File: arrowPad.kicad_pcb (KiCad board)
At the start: 2 copper layers, 28 parts, among them K1 KEYSW, K2 KEYSW, K3 KEYSW, K4 KEYSW, K5 KEYSW, K6 KEYSW, K7 KEYSW, K8 KEYSW, K9 KEYSW, SW1 SW_DIP_x01, U1 ProMicro, U2 NRF24L01_Breakout

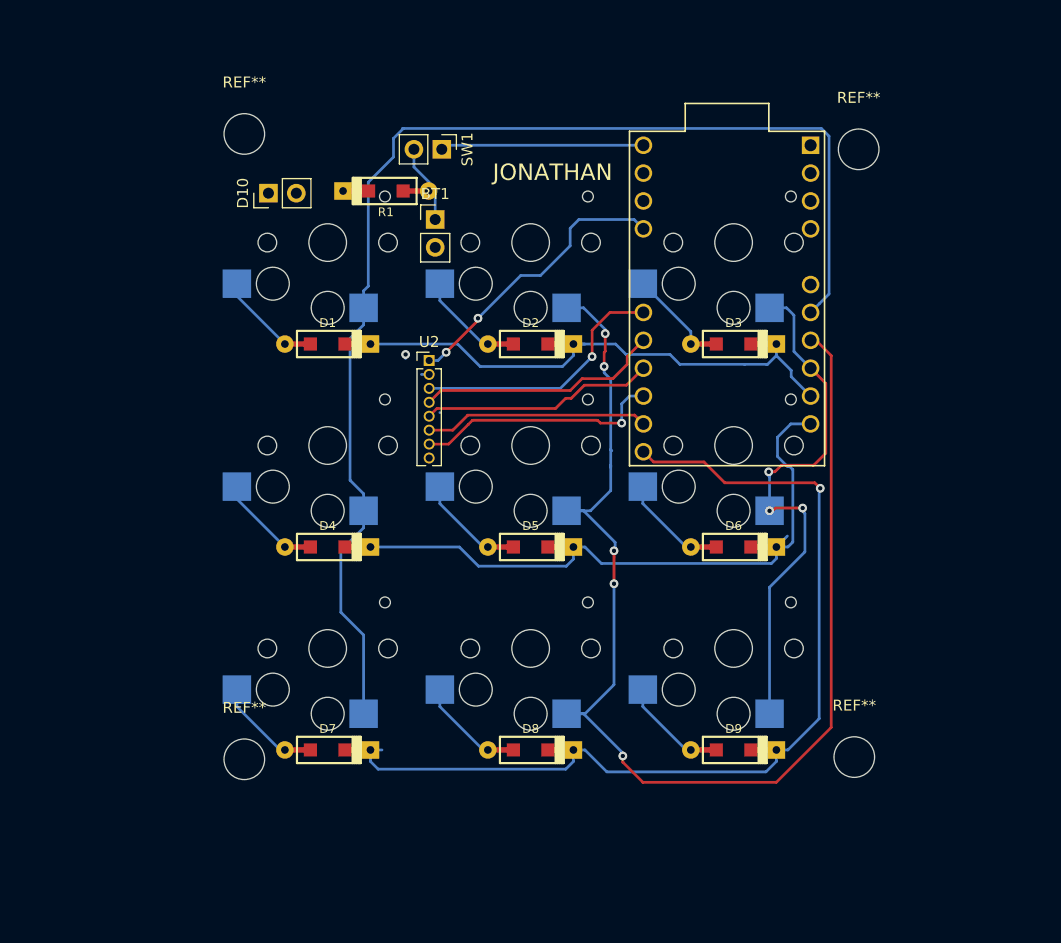
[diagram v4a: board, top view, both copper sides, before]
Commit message: added wired communication between boards
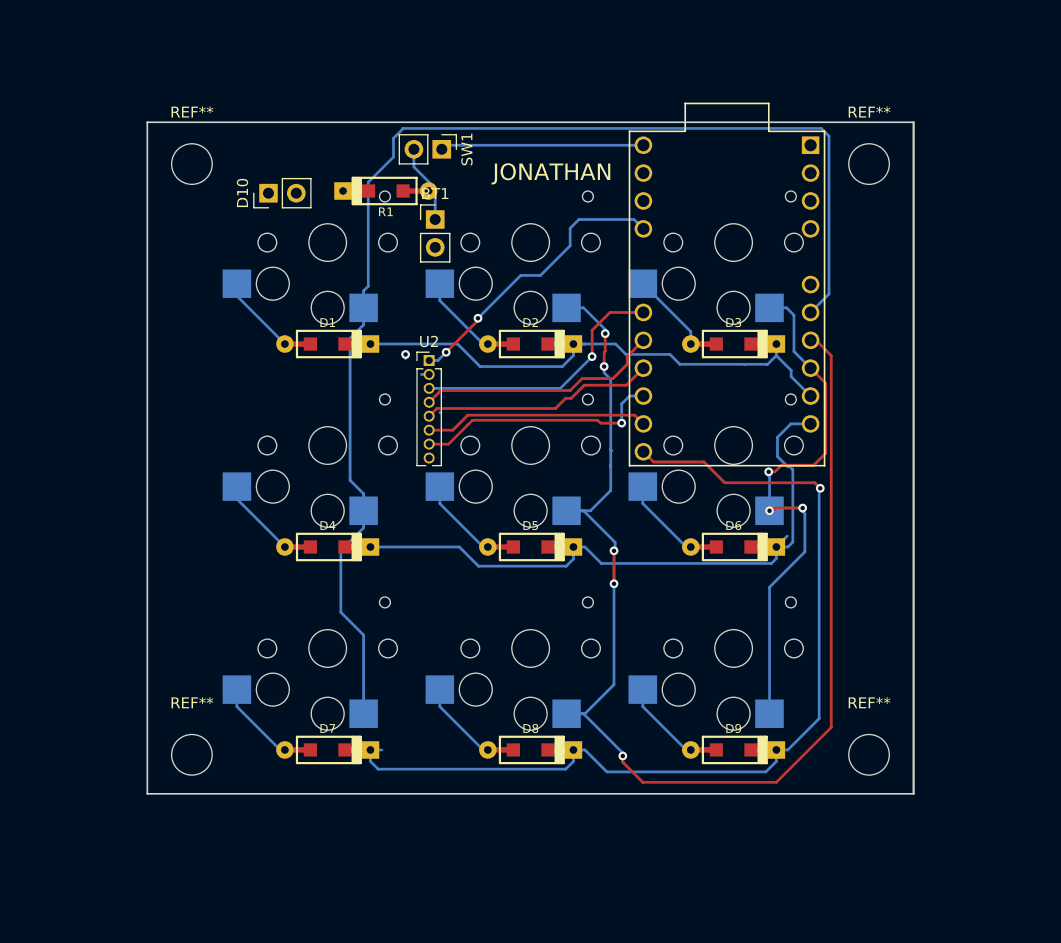
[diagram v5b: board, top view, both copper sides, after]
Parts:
- moved REF** 55.2 mm to (101.3, 139.2)
- moved REF** 54.1 mm to (101.3, 85.3)
- moved REF** 5.51 mm to (39.6, 85.3)
- moved REF** 4.79 mm to (39.6, 139.2)
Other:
- board outline added: 69.8 x 61.2 mm
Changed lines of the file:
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@@
-(kicad_pcb (version 20171130) (host pcbnew "(5.0.0-3-g5ebb6b6)")
+(kicad_pcb (version 20171130) (host pcbnew "(5.0.1)-4")
   (general
     (thickness 1.6)
-    (drawings 6)
+    (drawings 5)
     (tracks 227)
     (zones 0)
@@
     (pad_drill 0.762)
     (pad_to_mask_clearance 0.2)
+    (solder_mask_min_width 0.25)
     (aux_axis_origin 0 0)
-    (visible_elements FFFFFF7F)
+    (visible_elements 7FFFFFFF)
     (pcbplotparams
       (layerselection 0x010fc_ffffffff)
@@
     (add_net "Net-(U2-Pad8)")
   )
+  (module MountingHole:MountingHole_3.7mm (layer F.Cu)
+    (at 101.346 139.192)
+    (descr "Mounting Hole 3.7mm, no annular")
+    (tags "mounting hole 3.7mm no annular")
+    (attr virtual)
+    (fp_text reference REF** (at 0 -4.7) (layer F.SilkS)
+      (effects (font (size 1 1) (thickness 0.15)))
+    )
+    (fp_text value MountingHole_3.7mm (at 0 4.7) (layer F.Fab)
+      (effects (font (size 1 1) (thickness 0.15)))
+    )
+    (fp_text user %R (at 0.3 0) (layer F.Fab)
+      (effects (font (size 1 1) (thickness 0.15)))
+    )
+    (fp_circle (center 0 0) (end 3.7 0) (layer Cmts.User) (width 0.15))
+    (fp_circle (center 0 0) (end 3.95 0) (layer F.CrtYd) (width 0.05))
+    (pad 1 np_thru_hole circle (at 0 0) (size 3.7 3.7) (drill 3.7) (layers *.Cu *.Mask))
+  )
   (module Connector_PinHeader_2.54mm:PinHeader_1x02_P2.54mm_Vertical (layer F.Cu)
     (at 61.8 90.4)
@@
   )
   (module MountingHole:MountingHole_3.7mm (layer F.Cu)
-    (at 44.4 82.6)
+    (at 39.624 85.344)
     (descr "Mounting Hole 3.7mm, no annular")
     (tags "mounting hole 3.7mm no annular")
@@
   )
   (module MountingHole:MountingHole_3.7mm (layer F.Cu)
-    (at 44.4 139.6)
+    (at 39.624 139.192)
     (descr "Mounting Hole 3.7mm, no annular")
     (tags "mounting hole 3.7mm no annular")
@@
   )
   (module MountingHole:MountingHole_3.7mm (layer F.Cu)
-    (at 100.4 84)
+    (at 101.346 85.344)
     (descr "Mounting Hole 3.7mm, no annular")
     (tags "mounting hole 3.7mm no annular")
@@
     (pad 1 np_thru_hole circle (at 0 0) (size 3.7 3.7) (drill 3.7) (layers *.Cu *.Mask))
   )
-  (module MountingHole:MountingHole_3.7mm (layer F.Cu)
-    (at 100 139.4)
-    (descr "Mounting Hole 3.7mm, no annular")
-    (tags "mounting hole 3.7mm no annular")
-    (attr virtual)
-    (fp_text reference REF** (at 0 -4.7) (layer F.SilkS)
-      (effects (font (size 1 1) (thickness 0.15)))
-    )
-    (fp_text value MountingHole_3.7mm (at 0 4.7) (layer F.Fab)
-      (effects (font (size 1 1) (thickness 0.15)))
-    )
-    (fp_circle (center 0 0) (end 3.95 0) (layer F.CrtYd) (width 0.05))
-    (fp_circle (center 0 0) (end 3.7 0) (layer Cmts.User) (width 0.15))
-    (fp_text user %R (at 0.3 0) (layer F.Fab)
-      (effects (font (size 1 1) (thickness 0.15)))
-    )
-    (pad 1 np_thru_hole circle (at 0 0) (size 3.7 3.7) (drill 3.7) (layers *.Cu *.Mask))
-  )
-  (dimension 7 (width 0.3) (layer F.SilkS)
-    (gr_text "7.000 mm" (at 40.9 66.9) (layer F.SilkS)
-      (effects (font (size 1.5 1.5) (thickness 0.3)))
-    )
-    (feature1 (pts (xy 37.4 85.8) (xy 37.4 68.413579)))
-    (feature2 (pts (xy 44.4 85.8) (xy 44.4 68.413579)))
-    (crossbar (pts (xy 44.4 69) (xy 37.4 69)))
-    (arrow1a (pts (xy 37.4 69) (xy 38.526504 68.413579)))
-    (arrow1b (pts (xy 37.4 69) (xy 38.526504 69.586421)))
-    (arrow2a (pts (xy 44.4 69) (xy 43.273496 68.413579)))
-    (arrow2b (pts (xy 44.4 69) (xy 43.273496 69.586421)))
-  )
-  (dimension 7 (width 0.3) (layer F.SilkS)
-    (gr_text "7.000 mm" (at 100.1 71.7) (layer F.SilkS)
-      (effects (font (size 1.5 1.5) (thickness 0.3)))
-    )
-    (feature1 (pts (xy 103.6 93) (xy 103.6 73.213579)))
-    (feature2 (pts (xy 96.6 93) (xy 96.6 73.213579)))
-    (crossbar (pts (xy 96.6 73.8) (xy 103.6 73.8)))
-    (arrow1a (pts (xy 103.6 73.8) (xy 102.473496 74.386421)))
-    (arrow1b (pts (xy 103.6 73.8) (xy 102.473496 73.213579)))
-    (arrow2a (pts (xy 96.6 73.8) (xy 97.726504 74.386421)))
-    (arrow2b (pts (xy 96.6 73.8) (xy 97.726504 73.213579)))
-  )
-  (dimension 7 (width 0.3) (layer F.SilkS)
-    (gr_text "7.000 mm" (at 108.5 81.5 90) (layer F.SilkS)
-      (effects (font (size 1.5 1.5) (thickness 0.3)))
-    )
-    (feature1 (pts (xy 82.2 78) (xy 106.986421 78)))
-    (feature2 (pts (xy 82.2 85) (xy 106.986421 85)))
-    (crossbar (pts (xy 106.4 85) (xy 106.4 78)))
-    (arrow1a (pts (xy 106.4 78) (xy 106.986421 79.126504)))
-    (arrow1b (pts (xy 106.4 78) (xy 105.813579 79.126504)))
-    (arrow2a (pts (xy 106.4 85) (xy 106.986421 83.873496)))
-    (arrow2b (pts (xy 106.4 85) (xy 105.813579 83.873496)))
-  )
-  (dimension 7 (width 0.3) (layer F.SilkS)
-    (gr_text "7.000 mm" (at 22.1 140.5 270) (layer F.SilkS)
-      (effects (font (size 1.5 1.5) (thickness 0.3)))
-    )
-    (feature1 (pts (xy 65.2 144) (xy 23.613579 144)))
-    (feature2 (pts (xy 65.2 137) (xy 23.613579 137)))
-    (crossbar (pts (xy 24.2 137) (xy 24.2 144)))
-    (arrow1a (pts (xy 24.2 144) (xy 23.613579 142.873496)))
-    (arrow1b (pts (xy 24.2 144) (xy 24.786421 142.873496)))
-    (arrow2a (pts (xy 24.2 137) (xy 23.613579 138.126504)))
-    (arrow2b (pts (xy 24.2 137) (xy 24.786421 138.126504)))
-  )
-  (dimension 7 (width 0.3) (layer F.SilkS)
-    (gr_text "7.000 mm" (at 100.1 157.9) (layer F.SilkS)
-      (effects (font (size 1.5 1.5) (thickness 0.3)))
-    )
-    (feature1 (pts (xy 103.6 122.2) (xy 103.6 156.386421)))
-    (feature2 (pts (xy 96.6 122.2) (xy 96.6 156.386421)))
-    (crossbar (pts (xy 96.6 155.8) (xy 103.6 155.8)))
-    (arrow1a (pts (xy 103.6 155.8) (xy 102.473496 156.386421)))
-    (arrow1b (pts (xy 103.6 155.8) (xy 102.473496 155.213579)))
-    (arrow2a (pts (xy 96.6 155.8) (xy 97.726504 156.386421)))
-    (arrow2b (pts (xy 96.6 155.8) (xy 97.726504 155.213579)))
-  )
+  (gr_line (start 105.41 81.534) (end 105.41 142.748) (layer Edge.Cuts) (width 0.2))
+  (gr_line (start 35.56 142.748) (end 105.41 142.748) (layer Edge.Cuts) (width 0.15))
+  (gr_line (start 35.56 81.534) (end 35.56 142.748) (layer Edge.Cuts) (width 0.15))
+  (gr_line (start 105.41 81.534) (end 35.56 81.534) (layer Edge.Cuts) (width 0.15))
   (gr_text JONATHAN (at 72.5 86.1) (layer F.SilkS)
     (effects (font (size 1.5 1.5) (thickness 0.3)))

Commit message: final v1
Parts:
- removed the REF** at (101.3, 139.2)
- removed the REF** at (39.6, 85.3)
- removed the REF** at (39.6, 139.2)
- removed the REF** at (101.3, 85.3)
- removed SW1: SW_DIP_x01, Connector_PinHeader_2.54mm:PinHeader_1x02_P2.54mm_Vertical
- added J1: AudioJack3_Ground, Connector_PinHeader_2.54mm:PinHeader_1x04_P2.54mm_Vertical, F.Cu at (42.2, 108.6)
- added J2: AudioJack3_Ground, Connector_PinHeader_2.54mm:PinHeader_1x04_P2.54mm_Vertical, F.Cu at (98.8, 123.8)
- added REF**: MountingHole_3.5mm, MountingHole:MountingHole_3.5mm, F.Cu at (101.5, 85.5)
- added REF**: MountingHole_3.5mm, MountingHole:MountingHole_3.5mm, F.Cu at (39.5, 85.4)
- added REF**: MountingHole_3.5mm, MountingHole:MountingHole_3.5mm, F.Cu at (101.6, 142.2)
- added REF**: MountingHole_3.5mm, MountingHole:MountingHole_3.5mm, F.Cu at (39.4, 142.2)
- added U3: ADG417BN, Connector_PinHeader_2.54mm:PinHeader_1x03_P2.54mm_Vertical, F.Cu at (72.7, 83.3)
- moved R1 5.24 mm to (54.7, 83.2), turned to 180 degrees
- moved D10 4.85 mm to (45.0, 83.4)
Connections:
- R1 pad 1: Net-(D10-Pad2) -> Net-(R1-Pad1)
- R1 pad 2: Net-(R1-Pad2) -> Net-(D10-Pad2)
- U1 pad 6: Net-(R1-Pad2) -> /Col1
- U1 pad 7: /Col1 -> Net-(R1-Pad1)
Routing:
- net Net-(J1-Pad1): track 0.00 -> 151.5 mm, vias 0 -> 2
- net Net-(J1-Pad2): track 0.00 -> 145.8 mm
- net Net-(J1-Pad3): track 26.3 -> 90.8 mm, vias 2 -> 4
- net /RAW1: track 18.5 -> 81.0 mm, vias 0 -> 1
- net Net-(R1-Pad1): track 0.00 -> 49.9 mm
- net /Col1: track 113.5 -> 100.8 mm, vias 0 -> 2
- net Net-(D10-Pad2): track 0.00 -> 3.41 mm
- net Net-(BT1-Pad1): track 7.20 -> 10.2 mm
- net /Row2: track 57.8 -> 56.4 mm
- net /Col2: track 114.3 -> 115.3 mm
- added copper zone on F.Cu, net /GND1
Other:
- board size 69.8 x 61.2 mm -> 76.2 x 64.8 mm
- board text removed: "JONATHAN"
